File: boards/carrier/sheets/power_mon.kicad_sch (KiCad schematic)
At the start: 2 parts, among them U1 INA226AIDGSR

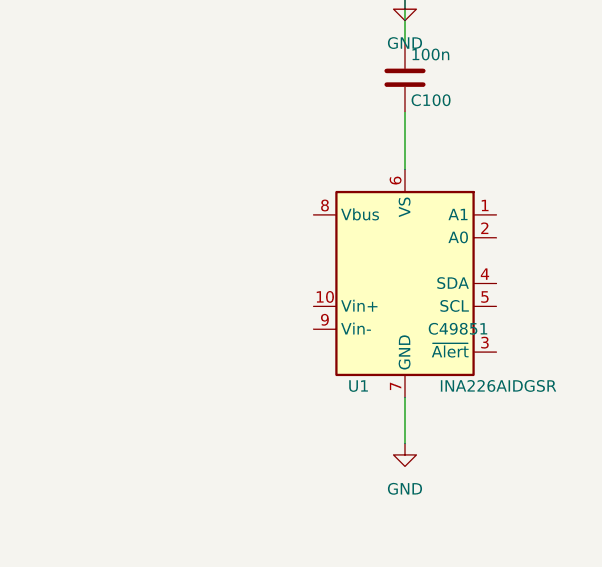
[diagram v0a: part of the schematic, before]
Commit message: place: auto-NC every IC pin not handled by overrides/cluster/power-paths
Default policy reversed: instead of NC'ing only pins explicitly listed
in the refcircuit's no_external_required, NC every IC pin we didn't
explicitly wire. A pin is "handled" if any of: pin_net_overrides /
net_overrides claim it, the cluster pass placed a passive against it,
it's the IC's primary supply pin (power_input_net / power_output_net
standard names), or it's a GND-family pin _attach_ic_ground covers.

Drops pin_not_connected ERC errors from ~45 → ~5 across the carrier
without requiring refcircuits to explicitly catalogue every unused pin
on every IC's symbol. A small visual cost (X mark on otherwise-bare
pins) for a clean baseline; refcircuits can still add explicit pin
handling when they want a nicer rendering.

  Before: 89 errors
  After:  44 errors
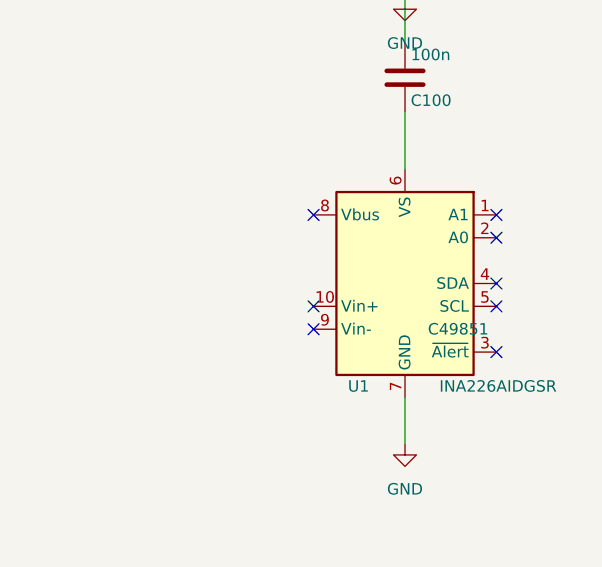
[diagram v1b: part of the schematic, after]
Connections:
- no-connect marks 0 -> 8
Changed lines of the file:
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@@
 		(instances
 			(project "Power Monitoring (INA226 on +VIN)"
-				(path "/d5ce81cb-67bf-4e2d-b9a0-1971845a1b88"
+				(path "/6db61f1a-e30a-4f6b-9d6d-436fb5aed287"
 					(reference "U1")
 					(unit 1)
@@
 		(instances
 			(project "Power Monitoring (INA226 on +VIN)"
-				(path "/d5ce81cb-67bf-4e2d-b9a0-1971845a1b88"
+				(path "/6db61f1a-e30a-4f6b-9d6d-436fb5aed287"
 					(reference "C100")
 					(unit 1)
@@
 		(instances
 			(project "Power Monitoring (INA226 on +VIN)"
-				(path "/d5ce81cb-67bf-4e2d-b9a0-1971845a1b88"
+				(path "/6db61f1a-e30a-4f6b-9d6d-436fb5aed287"
 					(reference "#PWR100")
 					(unit 1)
@@
 		(instances
 			(project "Power Monitoring (INA226 on +VIN)"
-				(path "/d5ce81cb-67bf-4e2d-b9a0-1971845a1b88"
+				(path "/6db61f1a-e30a-4f6b-9d6d-436fb5aed287"
 					(reference "#PWR101")
 					(unit 1)
@@
 		(instances
 			(project "Power Monitoring (INA226 on +VIN)"
-				(path "/d5ce81cb-67bf-4e2d-b9a0-1971845a1b88"
+				(path "/6db61f1a-e30a-4f6b-9d6d-436fb5aed287"
 					(reference "#PWR102")
 					(unit 1)
@@
 		)
 	)
+	(no_connect
+		(at 139.7 52.07)
+	)
+	(no_connect
+		(at 139.7 54.61)
+	)
+	(no_connect
+		(at 139.7 67.31)
+	)
+	(no_connect
+		(at 139.7 59.69)
+	)
+	(no_connect
+		(at 139.7 62.23)
+	)
+	(no_connect
+		(at 119.38 52.07)
+	)
+	(no_connect
+		(at 119.38 64.77)
+	)
+	(no_connect
+		(at 119.38 62.23)
+	)
 	(sheet_instances
